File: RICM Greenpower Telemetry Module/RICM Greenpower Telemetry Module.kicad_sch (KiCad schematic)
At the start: 47 parts, among them J1 Jack-DC, J10 Conn_01x02_Female, J11 Conn_01x02_Female, J2 Conn_01x05_Female, J3 Conn_02x04_Counter_Clockwise, J4 Conn_01x03_Female, J5 Conn_01x03_Female, J6 Conn_01x02_Female, J7 Conn_01x02_Female, J8 Conn_01x02_Female, J9 Conn_01x04_Female, U1 XL2001E1, U2 Pico, U3 MPU_6050_module, U4 Adafruit_MicroSD_SPI_SDIO, U5 ADS7830

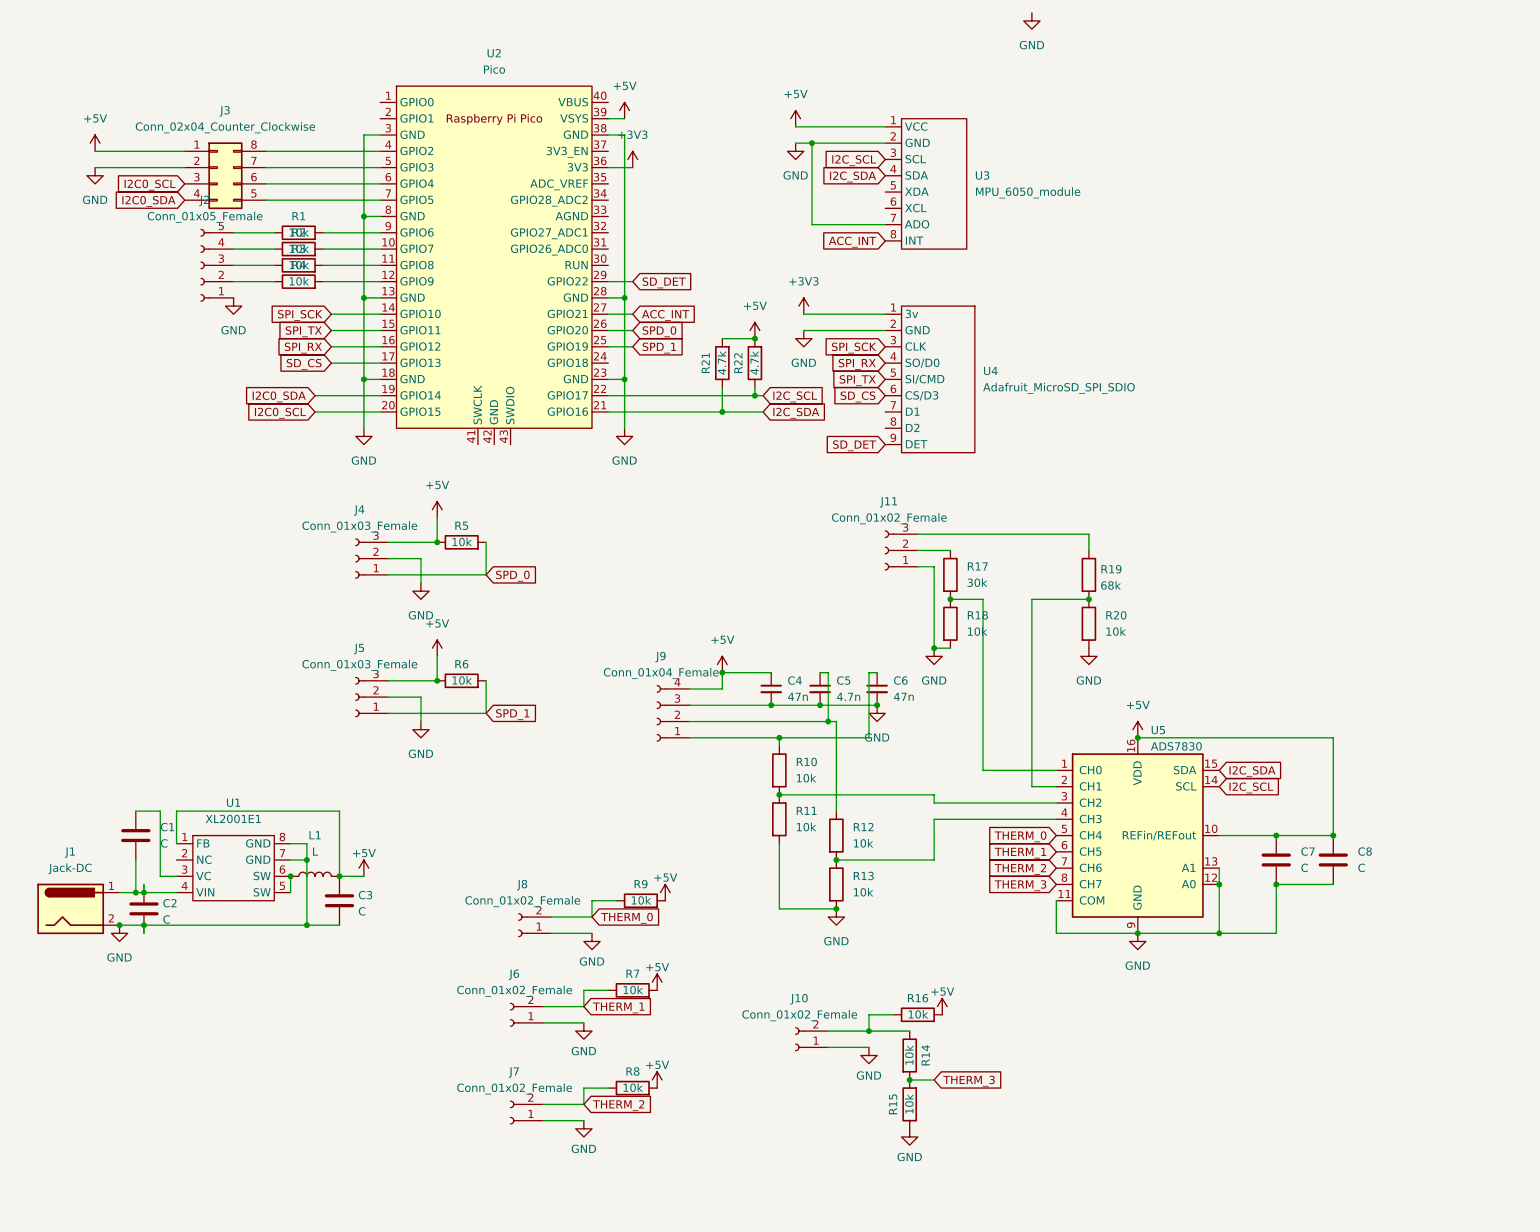
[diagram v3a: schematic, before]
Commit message: rearranged board
Switched to sdm resistors and capacitors. Added a 3v3 regulated supply. Various other revisions.
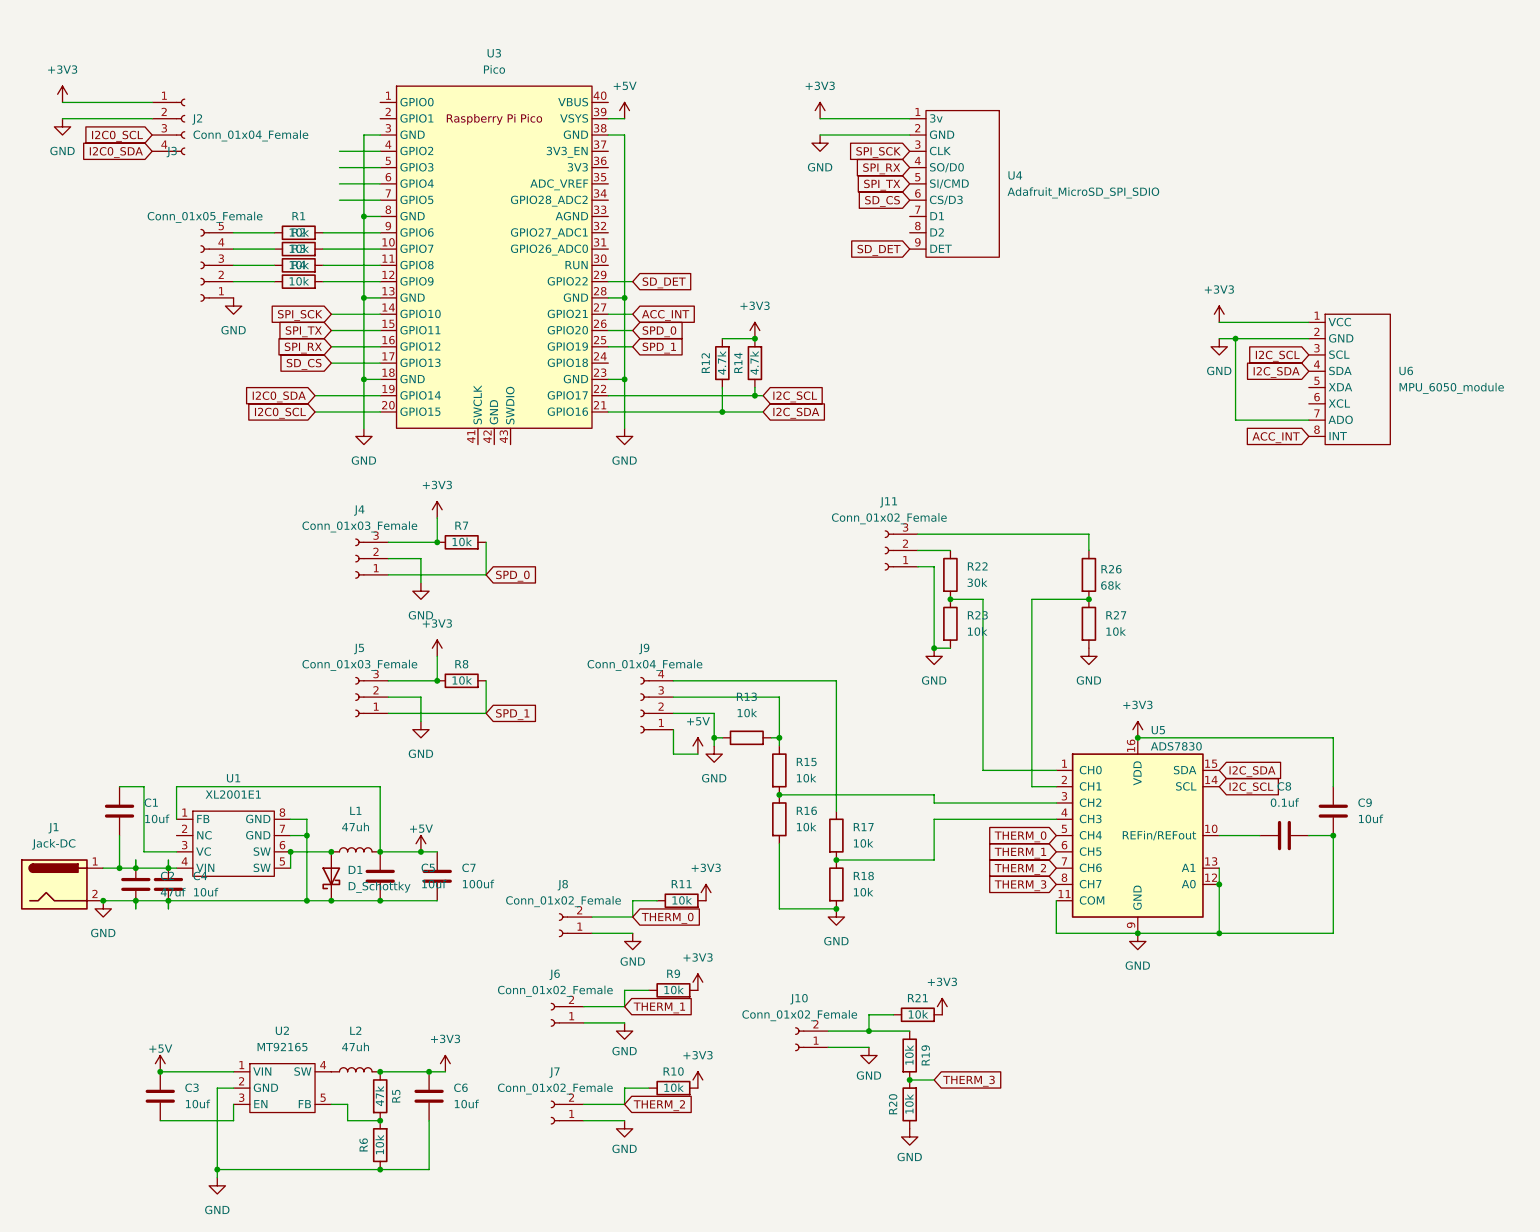
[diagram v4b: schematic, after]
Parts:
- removed C4, C6: 47n, Capacitor_THT:C_Disc_D4.7mm_W2.5mm_P5.00mm, symbol Device:C_Small
- removed C5: 4.7n, Capacitor_THT:C_Disc_D4.7mm_W2.5mm_P5.00mm, symbol Device:C_Small
- removed C7: C, Capacitor_THT:C_Disc_D5.0mm_W2.5mm_P5.00mm, symbol Device:C
- removed J3: Conn_02x04_Counter_Clockwise, Connector_PinHeader_2.54mm:PinHeader_2x04_P2.54mm_Vertical, symbol Connector_Generic:Conn_02x04_Counter_Clockwise
- added C3, C4, C5, C6, C9: 10uf, Capacitor_SMD:C_0805_2012Metric, symbol Device:C
- added D1: D_Schottky, Diode_SMD:D_SMA, symbol Device:D_Schottky
- added J2: Conn_01x04_Female, Connector_PinHeader_2.54mm:PinHeader_1x04_P2.54mm_Vertical, symbol Connector:Conn_01x04_Female
- added L2: 47uh, Inductor_THT:L_Axial_L12.0mm_D5.0mm_P15.24mm_Horizontal_Fastron_MISC, symbol Device:L
- added R13, R6: 10k, Resistor_SMD:R_1206_3216Metric, symbol Device:R
- added R5: 47k, Resistor_SMD:R_1206_3216Metric, symbol Device:R
- added U2: MT92165, Package_TO_SOT_SMD:SOT-23-5, symbol Converter_DCDC:MT92165
- C1: value C -> 10uf; footprint Capacitor_THT:C_Disc_D5.0mm_W2.5mm_P5.00mm -> Capacitor_SMD:C_0805_2012Metric
- C2: value C -> 47uf
- C7: renamed from C3; value C -> 100uf
- C8: value C -> 0.1uf; footprint Capacitor_THT:C_Disc_D5.0mm_W2.5mm_P5.00mm -> Capacitor_SMD:C_0805_2012Metric
- L1: value L -> 47uh; footprint Inductor_THT:L_Axial_L6.6mm_D2.7mm_P10.16mm_Horizontal_Vishay_IM-2 -> Inductor_THT:L_Axial_L12.0mm_D5.0mm_P15.24mm_Horizontal_Fastron_MISC
- R1, R2, R3, R4: footprint Resistor_THT:R_Axial_DIN0207_L6.3mm_D2.5mm_P7.62mm_Horizontal -> Resistor_SMD:R_1206_3216Metric
- R10: renamed from R8; footprint Resistor_THT:R_Axial_DIN0207_L6.3mm_D2.5mm_P7.62mm_Horizontal -> Resistor_SMD:R_1206_3216Metric
- R11: renamed from R9; footprint Resistor_THT:R_Axial_DIN0207_L6.3mm_D2.5mm_P7.62mm_Horizontal -> Resistor_SMD:R_1206_3216Metric
- R12: renamed from R21; footprint Resistor_THT:R_Axial_DIN0207_L6.3mm_D2.5mm_P7.62mm_Horizontal -> Resistor_SMD:R_1206_3216Metric
- R14: renamed from R22; footprint Resistor_THT:R_Axial_DIN0207_L6.3mm_D2.5mm_P7.62mm_Horizontal -> Resistor_SMD:R_1206_3216Metric
- R15: renamed from R10; footprint Resistor_THT:R_Axial_DIN0207_L6.3mm_D2.5mm_P7.62mm_Horizontal -> Resistor_SMD:R_1206_3216Metric
- R16: renamed from R11; footprint Resistor_THT:R_Axial_DIN0207_L6.3mm_D2.5mm_P7.62mm_Horizontal -> Resistor_SMD:R_1206_3216Metric
- R17: renamed from R12; footprint Resistor_THT:R_Axial_DIN0207_L6.3mm_D2.5mm_P7.62mm_Horizontal -> Resistor_SMD:R_1206_3216Metric
- R18: renamed from R13; footprint Resistor_THT:R_Axial_DIN0207_L6.3mm_D2.5mm_P7.62mm_Horizontal -> Resistor_SMD:R_1206_3216Metric
- R19: renamed from R14; footprint Resistor_THT:R_Axial_DIN0207_L6.3mm_D2.5mm_P7.62mm_Horizontal -> Resistor_SMD:R_1206_3216Metric
- R20: renamed from R15; footprint Resistor_THT:R_Axial_DIN0207_L6.3mm_D2.5mm_P7.62mm_Horizontal -> Resistor_SMD:R_1206_3216Metric
- R21: renamed from R16; footprint Resistor_THT:R_Axial_DIN0207_L6.3mm_D2.5mm_P7.62mm_Horizontal -> Resistor_SMD:R_1206_3216Metric
- R22: renamed from R17; footprint Resistor_THT:R_Axial_DIN0207_L6.3mm_D2.5mm_P7.62mm_Horizontal -> Resistor_SMD:R_1206_3216Metric
- R23: renamed from R18; footprint Resistor_THT:R_Axial_DIN0207_L6.3mm_D2.5mm_P7.62mm_Horizontal -> Resistor_SMD:R_1206_3216Metric
- R26: renamed from R19; footprint Resistor_THT:R_Axial_DIN0207_L6.3mm_D2.5mm_P7.62mm_Horizontal -> Resistor_SMD:R_1206_3216Metric
- R27: renamed from R20; footprint Resistor_THT:R_Axial_DIN0207_L6.3mm_D2.5mm_P7.62mm_Horizontal -> Resistor_SMD:R_1206_3216Metric
- R7: renamed from R5; footprint Resistor_THT:R_Axial_DIN0207_L6.3mm_D2.5mm_P7.62mm_Horizontal -> Resistor_SMD:R_1206_3216Metric
- R8: renamed from R6; footprint Resistor_THT:R_Axial_DIN0207_L6.3mm_D2.5mm_P7.62mm_Horizontal -> Resistor_SMD:R_1206_3216Metric
- R9: renamed from R7; footprint Resistor_THT:R_Axial_DIN0207_L6.3mm_D2.5mm_P7.62mm_Horizontal -> Resistor_SMD:R_1206_3216Metric
- renumbered J2 to J3, U2 to U3, U3 to U6
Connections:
- net +3V3: now also J4.3 (Pin_3), J5.3 (Pin_3), R10.2, R11.2, R12.2, R14.2, R21.2, R7.1, R8.1, R9.2, U5.16 (VDD), U6.1 (VCC), C6.1, C9.1, J2.1 (Pin_1), L2.2, R5.1; no longer U3.36 (3V3)
- net +5V: now also C7.1, J9.1 (Pin_1), C3.1, C5.1, U2.1 (VIN); no longer C7.2, C8.1, J4.3 (Pin_3), J5.3 (Pin_3), J9.4 (Pin_4), R10.2, R11.2, R12.2, R14.2, R21.2, R7.1, R8.1, R9.2, U5.10 (REFin/REFout), U5.16 (VDD), U6.1 (VCC)
- net GND: now also C7.2, J9.2 (Pin_2), C4.2, C5.2, C6.2, C9.2, D1.1 (K), J2.2 (Pin_2), R13.1, R6.1, U2.2 (GND); no longer C7.1, J9.3 (Pin_3)
- net I2C0_SCL: now also J2.3 (Pin_3)
- net I2C0_SDA: now also J2.4 (Pin_4)
- net at C1.2, C2.1, J1.1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: now also C4.1
- net at R15.1: now also J9.3 (Pin_3), R13.2; no longer J9.1 (Pin_1)
- net at R17.1: now also J9.4 (Pin_4); no longer J9.2 (Pin_2)
- net at L1.1, U1.5 (SW), U1.6 (SW): now also D1.2 (A)
- new net: R5.2, R6.2, U2.5 (FB)
- new net: C8.1, U5.10 (REFin/REFout)
- new net: C3.2, U2.3 (EN)
- new net: L2.1, U2.4 (SW)
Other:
- moved on the sheet: C1, C2, C7, J1, J6, J7, J8, J9, L1, R10, R11, R9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
